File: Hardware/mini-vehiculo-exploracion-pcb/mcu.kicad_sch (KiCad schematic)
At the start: 15 parts, among them J2 USB_C_Receptacle_USB2.0_16P, SW1 SW_Push

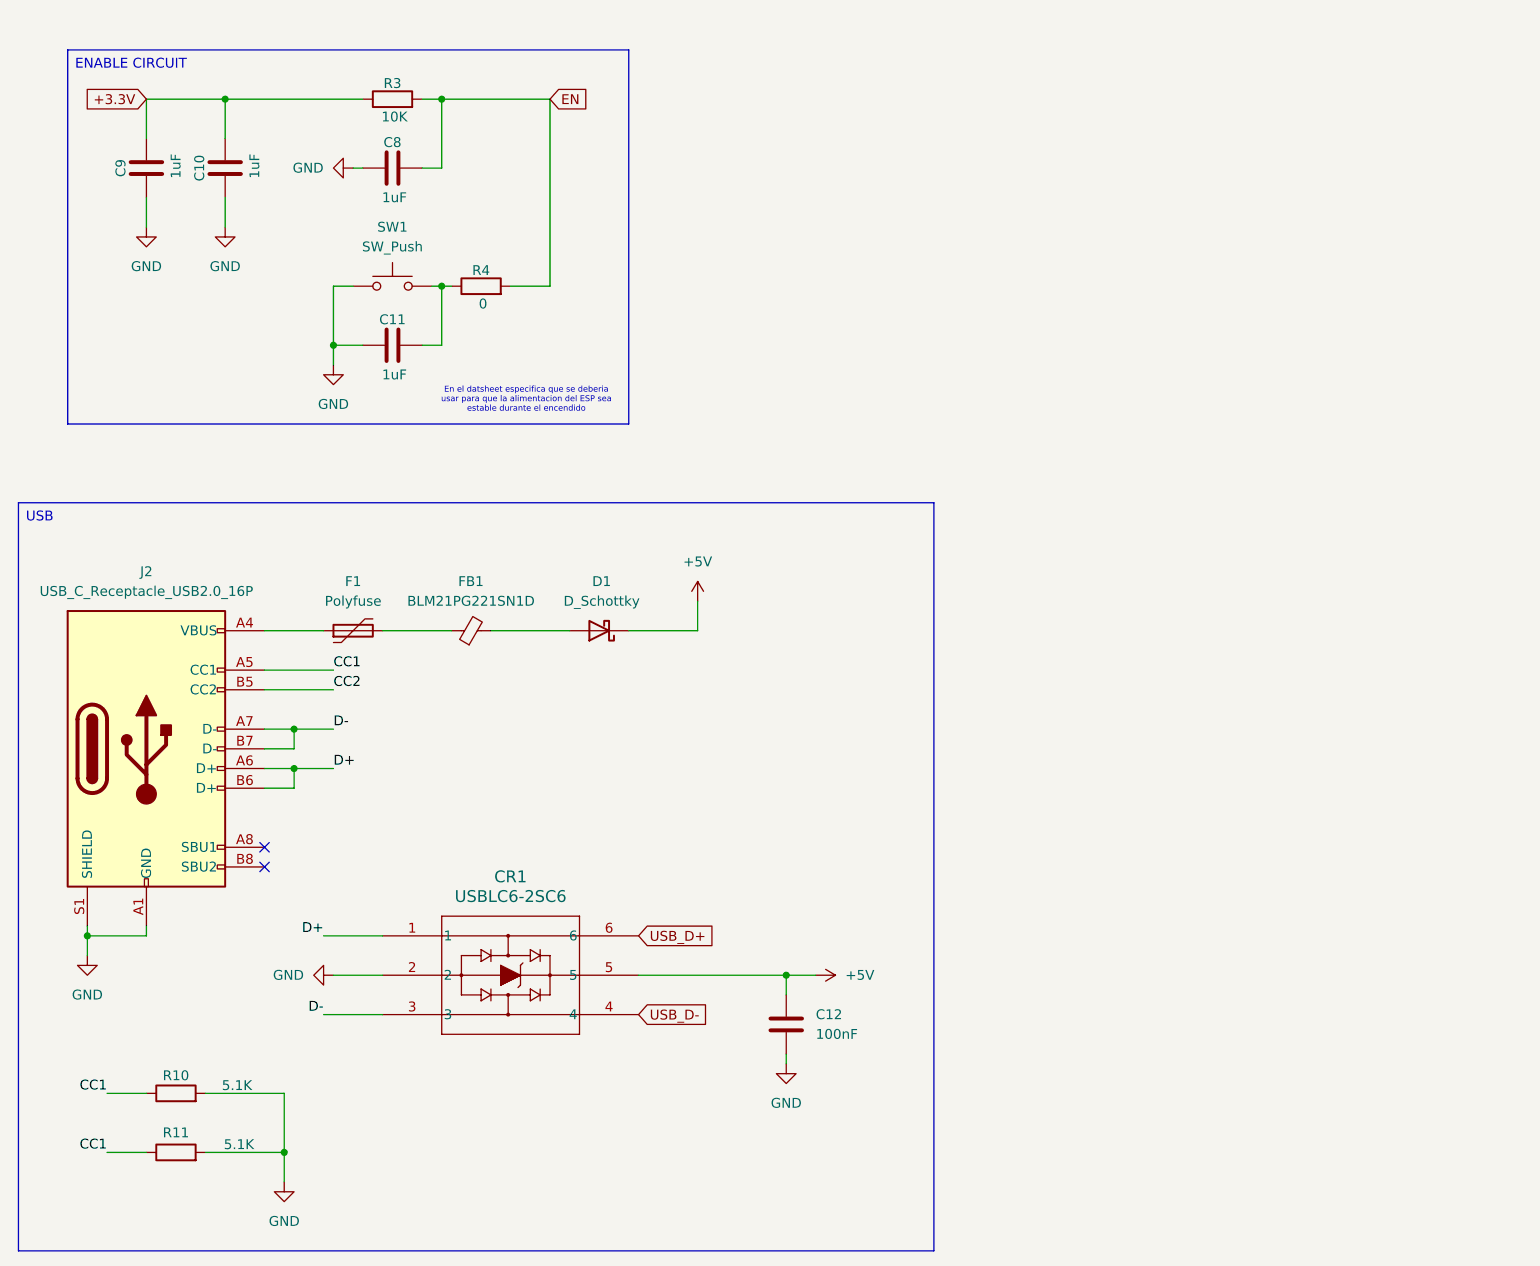
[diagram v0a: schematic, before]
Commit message: Add boot to the schematic
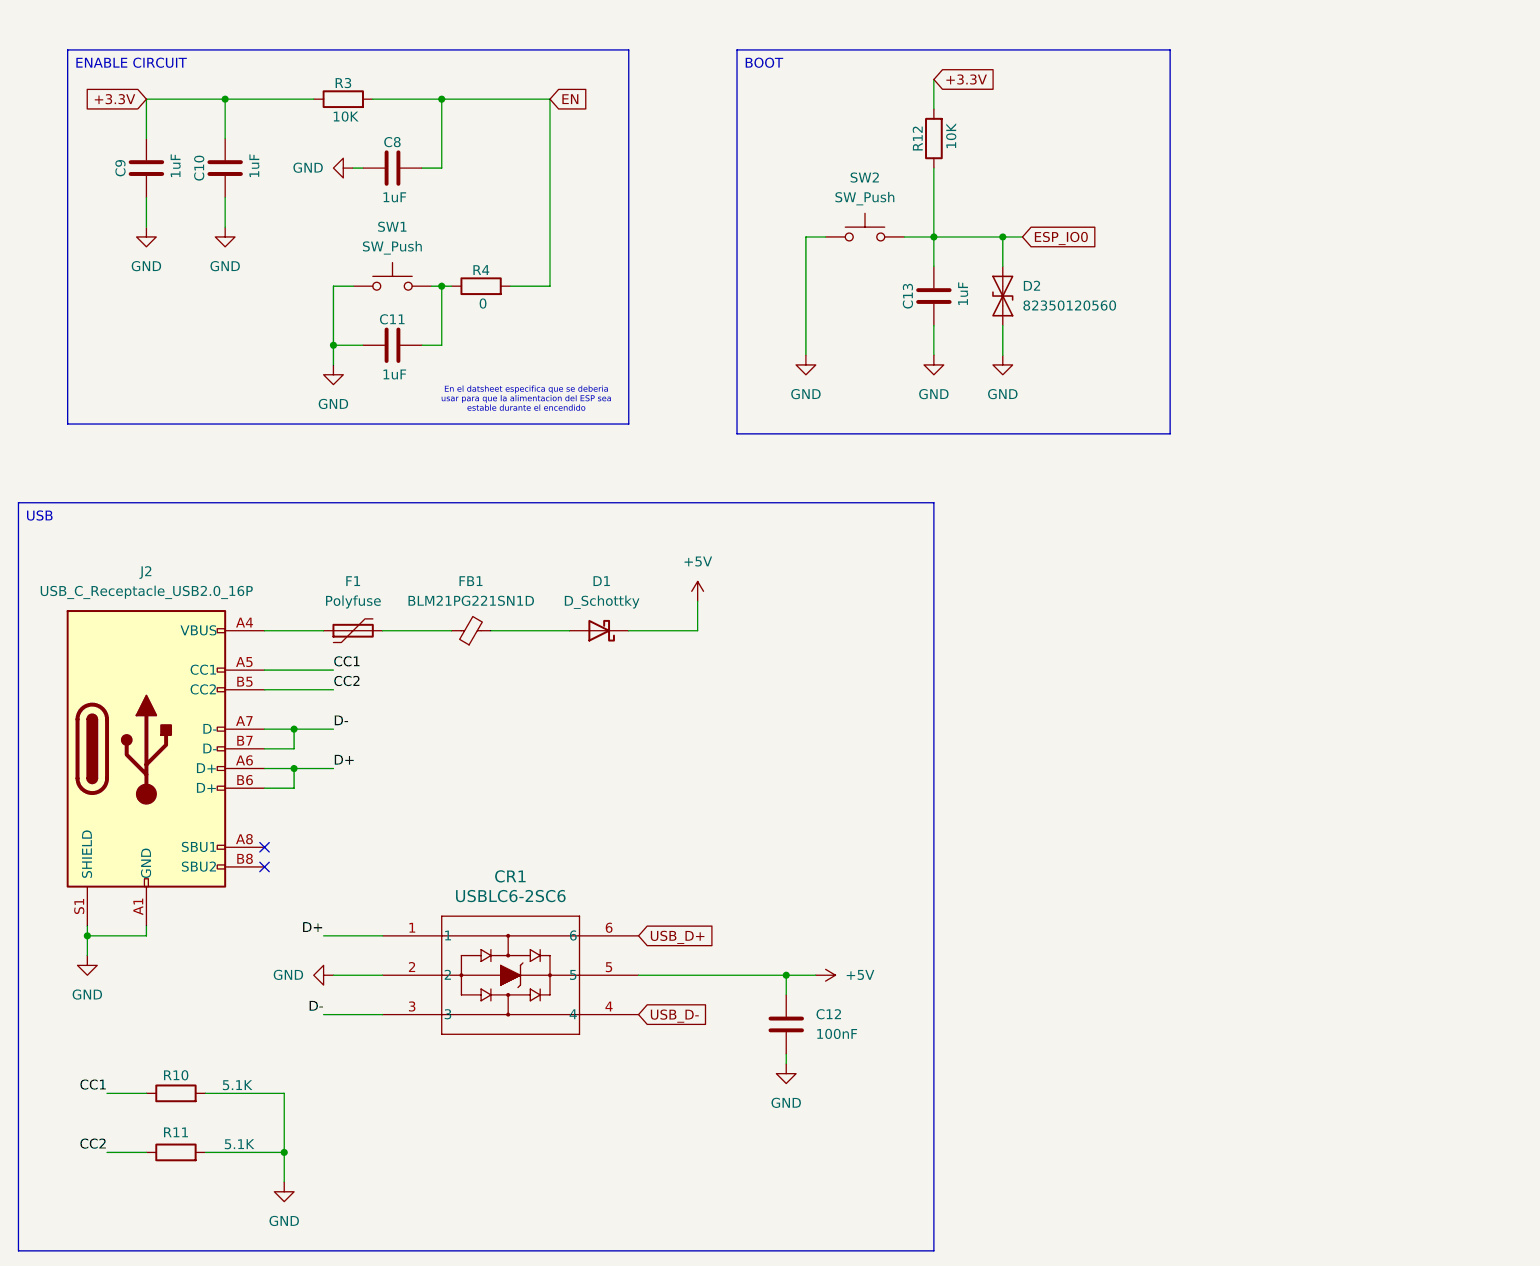
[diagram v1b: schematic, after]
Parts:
- added C13: 1uF, symbol Device:C
- added D2: 82350120560, symbol Diode:ESD9B3.3ST5G
- added R12: 10K, symbol Device:R
- added SW2: SW_Push, symbol Switch:SW_Push
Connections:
- net +3.3V: now also R12.2
- net CC1: no longer R11.1
- net CC2: now also R11.1
- net GND: now also C13.1, D2.1 (A1), SW2.1
- new net ESP_IO0: C13.2, D2.2 (A2), R12.1, SW2.2
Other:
- moved on the sheet: R3

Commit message: checking schematic/sheets
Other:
- note added: "Planilla OK"
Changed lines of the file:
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@@
 	(generator_version "9.0")
 	(paper "A4")
+	(text "Planilla OK"
+		(exclude_from_sim no)
+		(at 94.488 25.146 0)
+		(effects
+			(font
+				(size 1.27 1.27)
+				(color 245 0 255 1)
+			)
+		)
+	)
+	(text "Planilla OK"
+		(exclude_from_sim no)
+		(at 133.096 84.074 0)
+		(effects
+			(font
+				(size 1.27 1.27)
+				(color 245 0 255 1)
+			)
+		)
+	)
 	(text "En el datsheet especifica que se deberia \nusar para que la alimentacion del ESP sea \nestable durante el encendido"
 		(exclude_from_sim no)

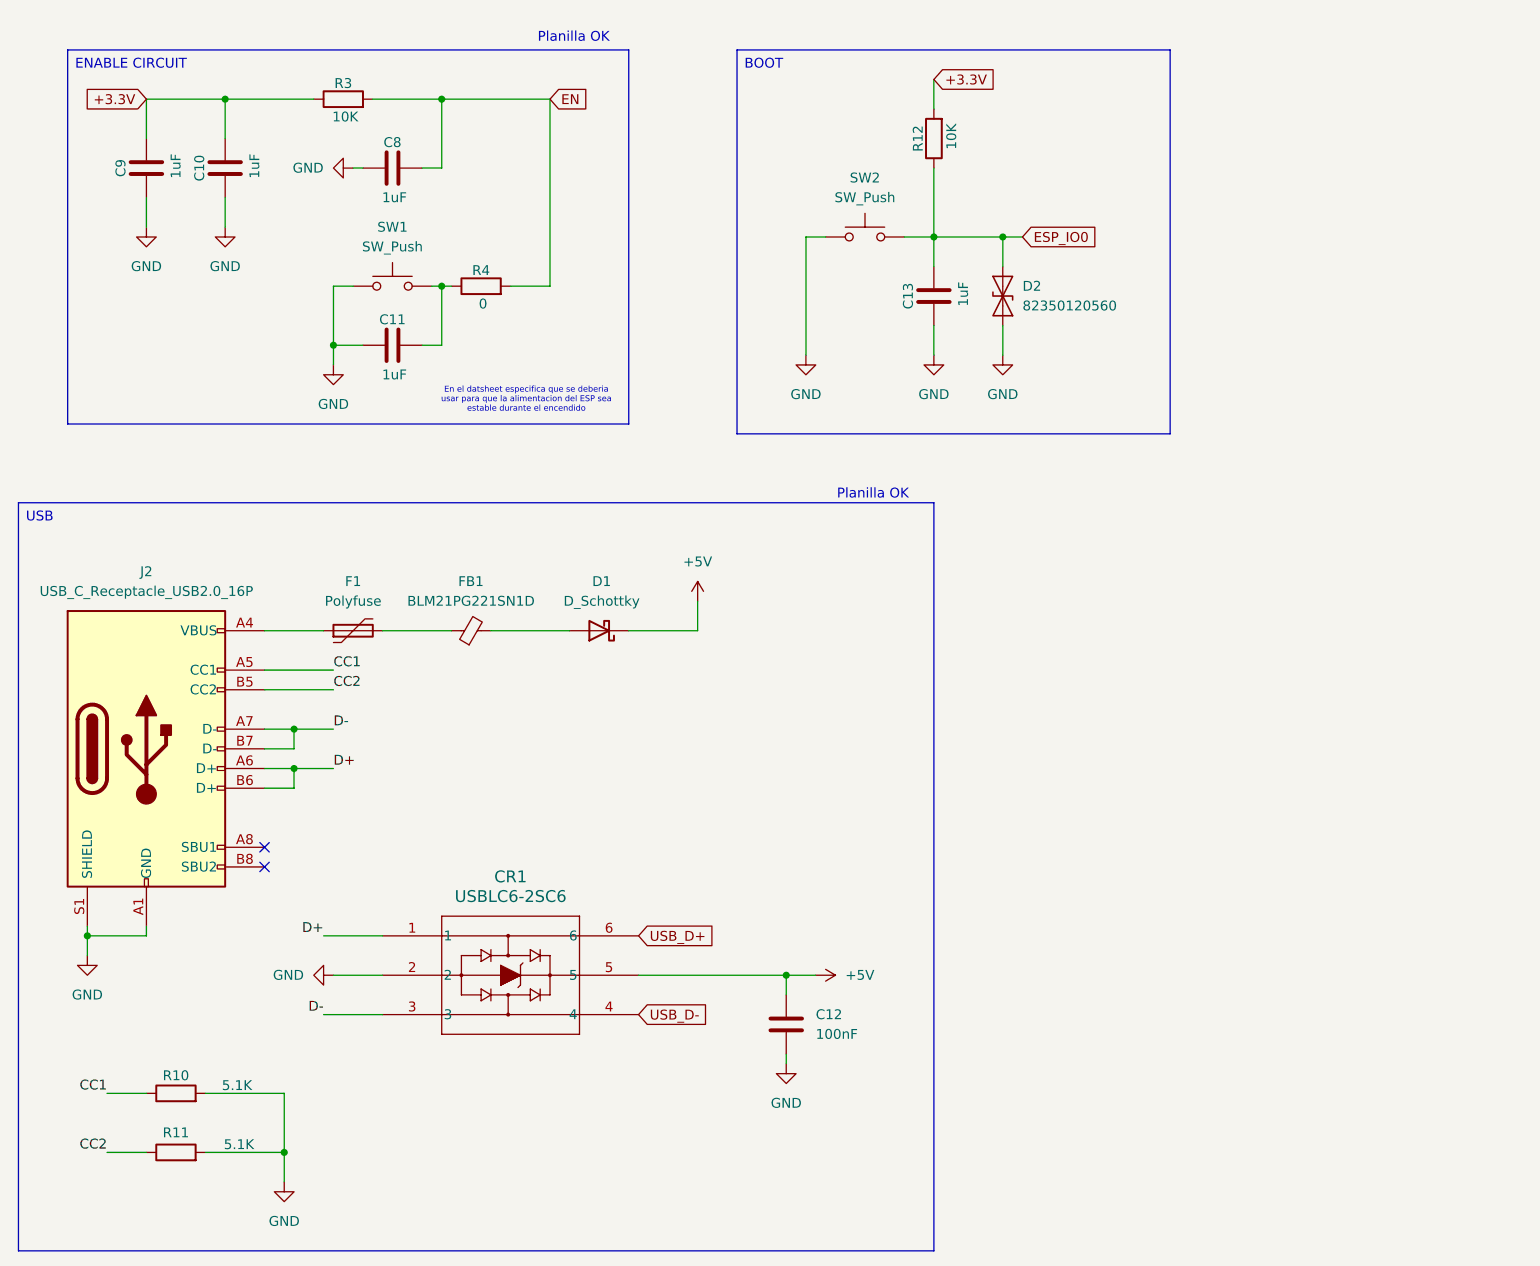
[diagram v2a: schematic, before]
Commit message: Update capacitor values
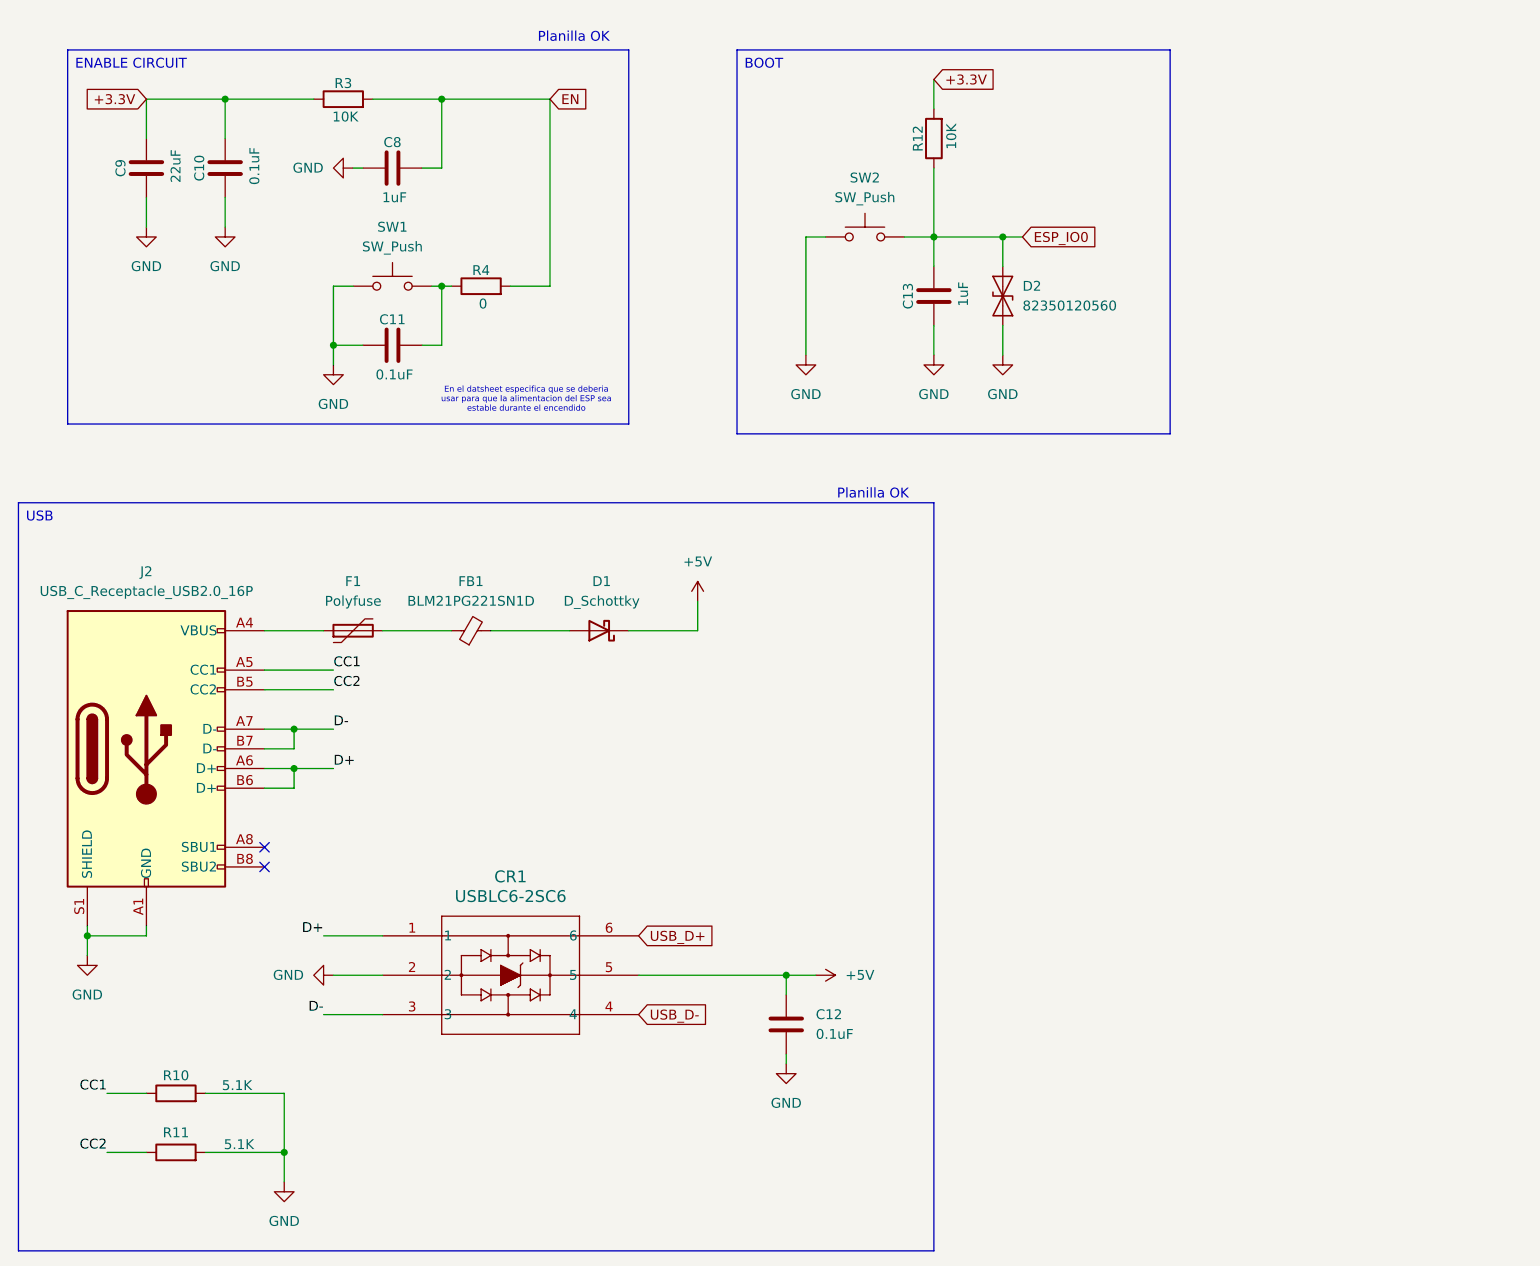
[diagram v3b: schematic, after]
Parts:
- C10, C11: value 1uF -> 0.1uF
- C12: value 100nF -> 0.1uF
- C9: value 1uF -> 22uF
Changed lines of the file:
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@@
 			)
 		)
-		(property "Value" "1uF"
+		(property "Value" "22uF"
 			(at 43.18 41.656 90)
 			(effects
@@
 			)
 		)
-		(property "Value" "100nF"
+		(property "Value" "0.1uF"
 			(at 125.73 153.6699 0)
 			(effects
@@
 			)
 		)
-		(property "Value" "1uF"
+		(property "Value" "0.1uF"
 			(at 71.374 68.58 90)
 			(effects
@@
 			)
 		)
-		(property "Value" "1uF"
+		(property "Value" "0.1uF"
 			(at 53.34 41.656 90)
 			(effects

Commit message: actualizacion labels pcb drivers
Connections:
- net +5V renamed V_BUS
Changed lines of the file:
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@@
+		)
+	)
+	(global_label "V_BUS"
+		(shape input)
+		(at 110.49 97.79 0)
+		(fields_autoplaced yes)
+		(effects
+			(font
+				(size 1.27 1.27)
+			)
+			(justify left)
+		)
+		(property "Intersheetrefs" "${INTERSHEET_REFS}"
+			(at 119.3414 97.79 0)
+			(effects
+				(font
+					(size 1.27 1.27)
+				)
+				(justify left)
+				(hide yes)
+			)
+		)
+	)
+	(global_label "V_BUS"
+		(shape input)
+		(at 125.73 146.05 0)
+		(fields_autoplaced yes)
+		(effects
+			(font
+				(size 1.27 1.27)
+			)
+			(justify left)
+		)
+		(property "Intersheetrefs" "${INTERSHEET_REFS}"
+			(at 134.5814 146.05 0)
+			(effects
+				(font
+					(size 1.27 1.27)
+				)
+				(justify left)
+				(hide yes)
+			)
 		)
 	)
@@
 	)
 	(symbol
-		(lib_id "power:+5V")
-		(at 125.73 146.05 270)
-		(unit 1)
-		(exclude_from_sim no)
-		(in_bom yes)
-		(on_board yes)
-		(dnp no)
-		(fields_autoplaced yes)
-		(property "Reference" "#PWR016"
-			(at 121.92 146.05 0)
-			(effects
-				(font
-					(size 1.27 1.27)
-				)
-				(hide yes)
-			)
-		)
-		(property "Value" "+5V"
-			(at 129.54 146.0499 90)
-			(effects
-				(font
-					(size 1.27 1.27)
-				)
-				(justify left)
-			)
-		)
-		(property "Footprint" ""
-			(at 125.73 146.05 0)
-			(effects
-				(font
-					(size 1.27 1.27)
-				)
-				(hide yes)
-			)
-		)
-		(property "Datasheet" ""
-			(at 125.73 146.05 0)
-			(effects
-				(font
-					(size 1.27 1.27)
-				)
-				(hide yes)
-			)
-		)
-		(property "Description" "Power symbol creates a global label with name \"+5V\""
-			(at 125.73 146.05 0)
-			(effects
-				(font
-					(size 1.27 1.27)
-				)
-				(hide yes)
-			)
-		)
-		(pin "1"
-		)
-		(instances
-			(project "mini-vehiculo-exploracion-pcb"
-				(path "/3cb3b833-c38f-47b4-b7e9-f0e6337b7613/7b198334-65f4-4536-9697-14ad78bccec0"
-					(reference "#PWR016")
-					(unit 1)
-				)
-			)
-		)
-	)
-	(symbol
 		(lib_id "power:GND")
 		(at 66.04 41.91 270)
@@
 					(unit 1)
 				)
-			)
-		)
-	)
-	(symbol
-		(lib_id "power:+5V")
-		(at 110.49 97.79 0)
-		(unit 1)
-		(exclude_from_sim no)
-		(in_bom yes)
-		(on_board yes)
-		(dnp no)
-		(fields_autoplaced yes)
-		(property "Reference" "#PWR013"
-			(at 110.49 101.6 0)
-			(effects
-				(font
-					(size 1.27 1.27)
-				)
-				(hide yes)
-			)
-		)
-		(property "Value" "+5V"
-			(at 110.49 92.71 0)
-			(effects
-				(font
-					(size 1.27 1.27)
-				)
-			)
-		)
-		(property "Footprint" ""
-			(at 110.49 97.79 0)
-			(effects
-				(font
-					(size 1.27 1.27)
-				)
-				(hide yes)
-			)
-		)
-		(property "Datasheet" ""
-			(at 110.49 97.79 0)
-			(effects
-				(font
-					(size 1.27 1.27)
-				)
-				(hide yes)
-			)
-		)
-		(property "Description" "Power symbol creates a global label with name \"+5V\""
-			(at 110.49 97.79 0)
-			(effects
-				(font
-					(size 1.27 1.27)
-				)
-				(hide yes)
-			)
-		)
-		(pin "1"
-		)
-		(instances
-			(project ""
-				(path "/3cb3b833-c38f-47b4-b7e9-f0e6337b7613/7b198334-65f4-4536-9697-14ad78bccec0"
-					(reference "#PWR013")
-					(unit 1)
-				)
